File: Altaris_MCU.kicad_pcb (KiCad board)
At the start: 2 copper layers, 101.9 x 50.1 mm, 61 parts, among them J1 Screw_Terminal_01x02, J2 Conn_01x04_Pin, J3 Screw_Terminal_01x02, J4 Screw_Terminal_01x02, J5 Conn_01x04_Pin, J6 Conn_01x04_Pin, J8 Screw_Terminal_01x02, J9 USB_C_Receptacle_USB2.0_16P, SW2 RESET1, SW3 BOOT1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

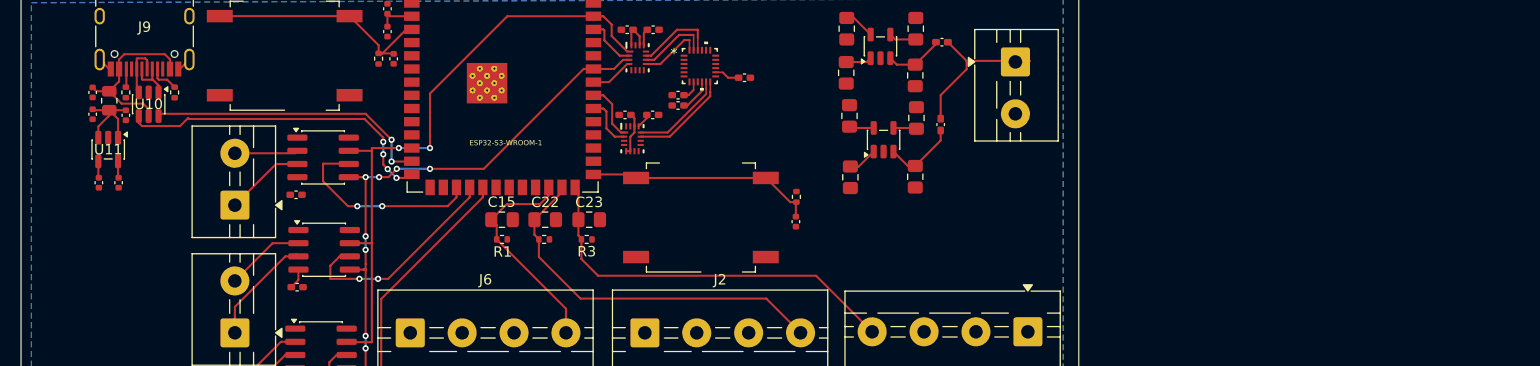
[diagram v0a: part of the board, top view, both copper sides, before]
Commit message: Swapped LDO for Buck and added some test LED's
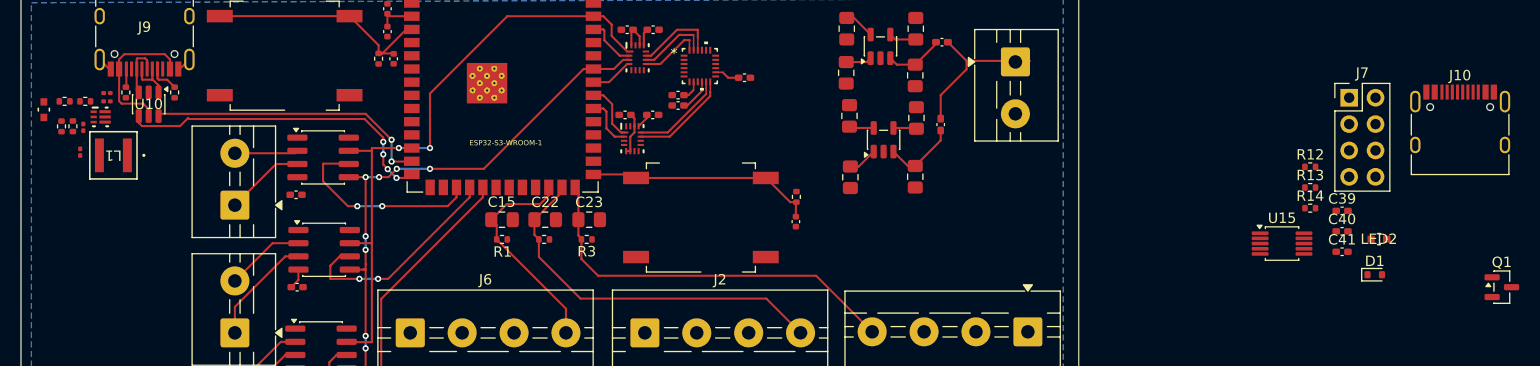
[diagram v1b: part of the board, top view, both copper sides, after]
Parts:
- removed C27, C28, C30: 10u, Capacitor_SMD:C_0402_1005Metric
- removed C29: 100n, Capacitor_SMD:C_0402_1005Metric
- removed FB3: 600/100, Resistor_SMD:R_0805_2012Metric
- removed U11: SPX3819M5-L-3-3, Package_TO_SOT_SMD:SOT-23-5
- added C31: 4.7u, Capacitor_SMD:C_0201_0603Metric, F.Cu at (116.4, 100.1)
- added C32: 30u, Capacitor_SMD:C_0201_0603Metric, F.Cu at (113.8, 105.8)
- added C33: 120p, Capacitor_SMD:C_0201_0603Metric, F.Cu at (114.1, 103.4)
- added C39: 0.1uF, Capacitor_SMD:C_0402_1005Metric_Pad0.74x0.62mm_HandSolder, F.Cu at (235.4, 111.5)
- added C40: 0.1uF, Capacitor_SMD:C_0402_1005Metric_Pad0.74x0.62mm_HandSolder, F.Cu at (235.4, 113.4)
- added C41: 0.1uF, Capacitor_SMD:C_0402_1005Metric_Pad0.74x0.62mm_HandSolder, F.Cu at (235.4, 115.4)
- added D1: 1N4148WT, Diode_SMD:D_SOD-523, F.Cu at (238.5, 117.6)
- added J10: USB_C_Receptacle_USB2.0_16P, Connector_USB:USB_C_Receptacle_HRO_TYPE-C-31-M-12, F.Cu at (246.7, 104.0)
- added J7: Conn_01x08_Socket, Connector_PinHeader_2.54mm:PinHeader_2x04_P2.54mm_Vertical, F.Cu at (236.1, 100.5)
- added L1: 0.47u, MyFootprints:IND_XFL4015_COC, F.Cu at (117.0, 106.1)
- added LED1: LTST-C190KRKT, MyFootprints:LED_LTST-C190_LTO, F.Cu at (110.3, 101.7)
- added LED2: LTST-C190KRKT, MyFootprints:LED_LTST-C190_LTO, F.Cu at (238.9, 114.2)
- added Q1: Q_NMOS, Package_TO_SOT_SMD:SOT-23, F.Cu at (250.8, 118.8)
- added R11: 1k, Resistor_SMD:R_0402_1005Metric, F.Cu at (112.3, 100.9)
- added R12: 1k, Resistor_SMD:R_0402_1005Metric, F.Cu at (232.3, 107.2)
- added R13: 5.1k, Resistor_SMD:R_0402_1005Metric, F.Cu at (232.3, 109.2)
- added R14: 5.1k, Resistor_SMD:R_0402_1005Metric, F.Cu at (232.3, 111.2)
- added R6: 100k, Resistor_SMD:R_0402_1005Metric, F.Cu at (114.3, 100.9)
- added R7: 450k, Resistor_SMD:R_0402_1005Metric, F.Cu at (113.1, 103.3)
- added R8: 100k, Resistor_SMD:R_0402_1005Metric, F.Cu at (112.0, 103.3)
- added U12: TPS62827DMQT, MyFootprints:DMQ0006A, F.Cu at (115.8, 102.4)
- added U15: CH340X, Package_SO:MSOP-10_3x3mm_P0.5mm, F.Cu at (229.6, 114.6)
- C26: value 100n -> 0.1u; footprint Capacitor_SMD:C_0402_1005Metric -> Capacitor_SMD:C_0201_0603Metric
- moved C26 1.63 mm to (116.4, 100.9), turned to 0 degrees
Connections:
- C26 pad 1: +VBUS -> GND
- C26 pad 2: GND -> Net-(U10-VBUS)
- J9 pad A4: +VBUS -> Net-(U10-VBUS)
- J9 pad A9: +VBUS -> Net-(U10-VBUS)
- J9 pad B4: +VBUS -> Net-(U10-VBUS)
- J9 pad B9: +VBUS -> Net-(U10-VBUS)
- U1 pad 23: unconnected-(U1-IO21-Pad23) -> TESTLED
- U1 pad 36: unconnected-(U1-RXD0-Pad36) -> RXD0
- U1 pad 37: unconnected-(U1-TXD0-Pad37) -> TXD0
- U10 pad 5: +VBUS -> Net-(U10-VBUS)
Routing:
- net +VBUS: track 16.6 -> 0.00 mm
- net Net-(U10-VBUS): track 0.00 -> 14.1 mm
- net +VBUSF: track 9.33 -> 0.00 mm
- net Net-(U11-BP): track 1.60 -> 0.00 mm
- net +3.3V_b: track 19.8 -> 18.2 mm

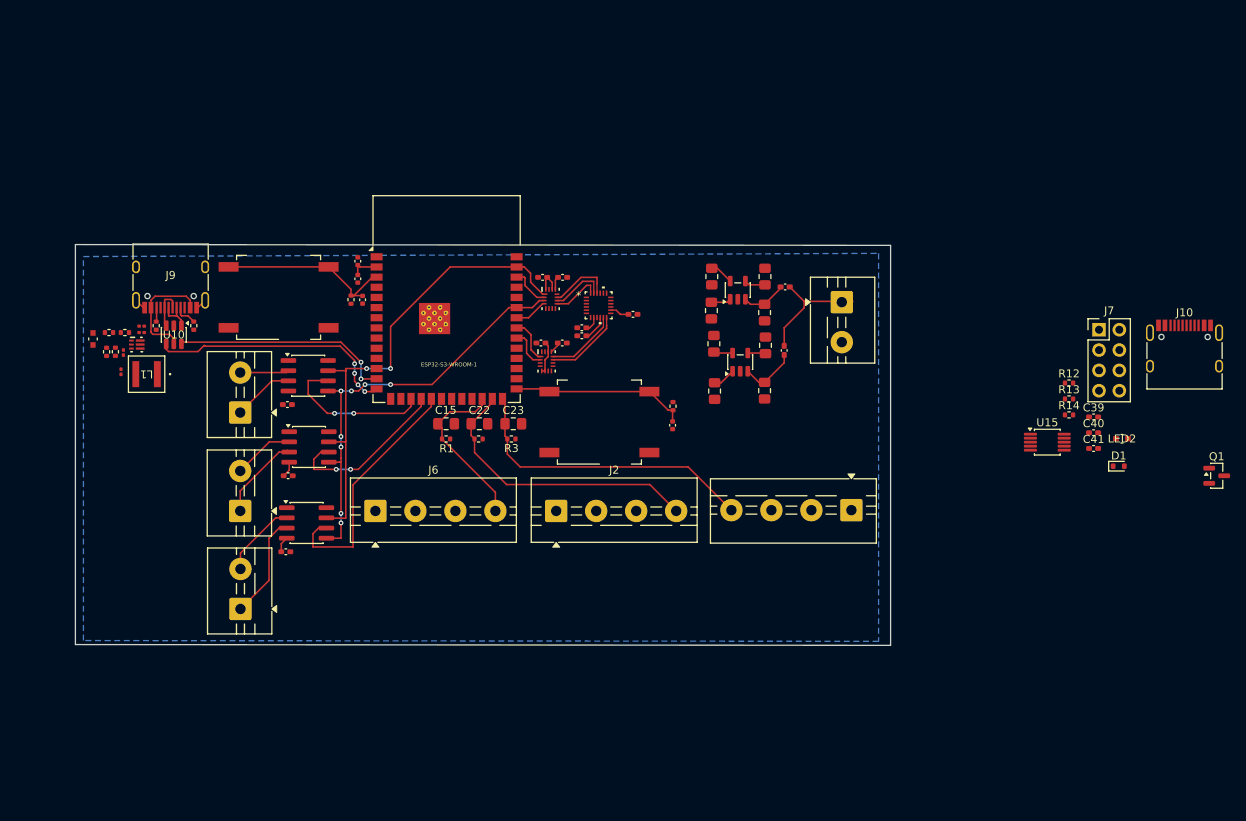
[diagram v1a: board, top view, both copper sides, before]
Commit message: Moved USB-C, Routed Buck converter output to LDO, Removed an LDO on PCB, Added another Thermocouple sensor
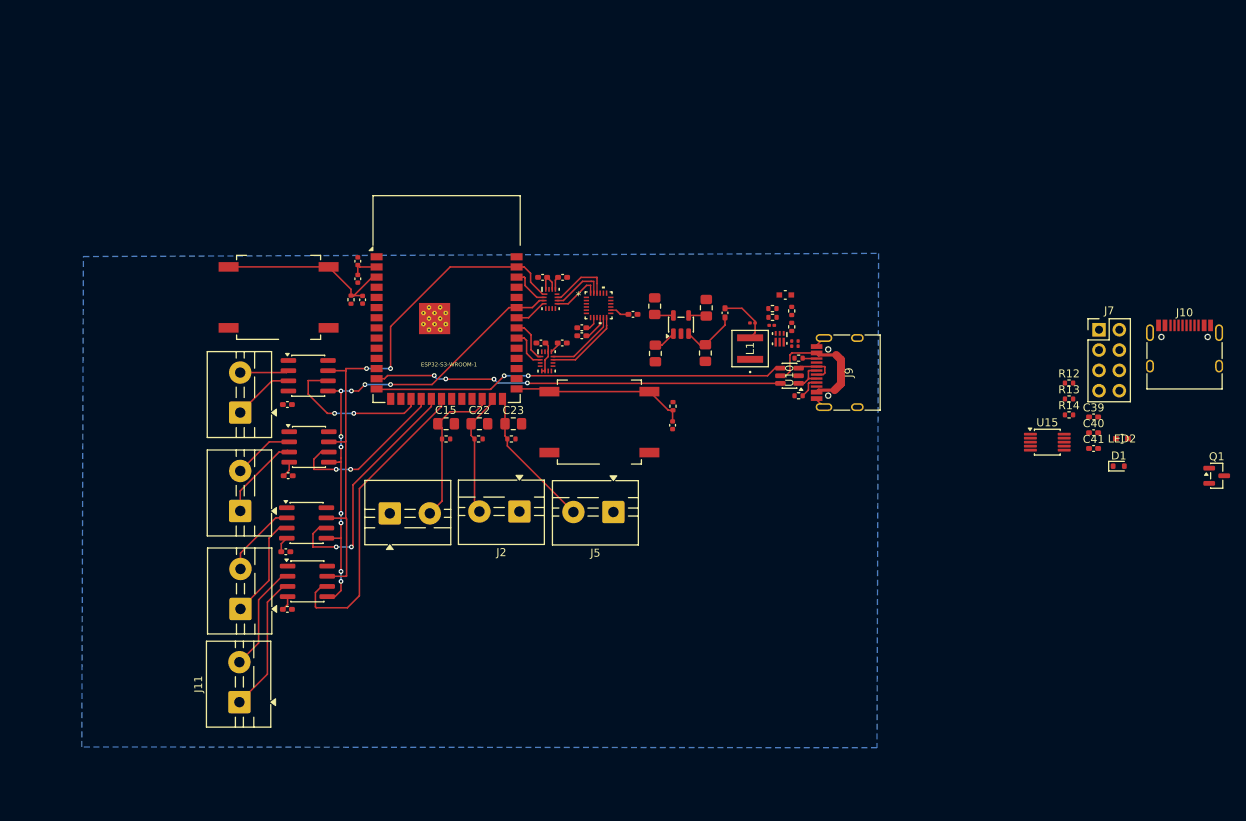
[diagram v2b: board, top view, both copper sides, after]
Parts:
- removed C1: 0.1uF, Capacitor_SMD:C_0805_2012Metric_Pad1.18x1.45mm_HandSolder
- removed C10, C7: 10uF, Capacitor_SMD:C_0805_2012Metric_Pad1.18x1.45mm_HandSolder
- removed C5: 0.01uF, Capacitor_SMD:C_0805_2012Metric_Pad1.18x1.45mm_HandSolder
- removed FB1: 220 @ 100MHz, Inductor_SMD:L_0402_1005Metric_Pad0.77x0.64mm_HandSolder
- removed J8: Screw_Terminal_01x02, TerminalBlock:TerminalBlock_MaiXu_MX126-5.0-02P_1x02_P5.00mm
- removed U3: TPS79333-EP, Package_TO_SOT_SMD:SOT-23-5
- added C27: 0.1uF, Capacitor_SMD:C_0402_1005Metric_Pad0.74x0.62mm_HandSolder, F.Cu at (134.6, 135.5)
- added J11: Screw_Terminal_01x02, TerminalBlock:TerminalBlock_MaiXu_MX126-5.0-02P_1x02_P5.00mm, F.Cu at (128.6, 147.1)
- added U11: MAX31855KASA, Package_SO:SOIC-8_3.9x4.9mm_P1.27mm, F.Cu at (137.1, 132.0)
- J2, J5, J6: footprint TerminalBlock:TerminalBlock_MaiXu_MX126-5.0-04P_1x04_P5.00mm -> TerminalBlock:TerminalBlock_MaiXu_MX126-5.0-02P_1x02_P5.00mm
- moved LED1 86.7 mm to (196.8, 96.2), turned to 0 degrees
- moved J9 85.7 mm to (204.8, 105.9), turned to 90 degrees
- moved R11 85.4 mm to (197.6, 98.2), turned to -90 degrees
- moved R8 83.4 mm to (195.2, 97.9), turned to 0 degrees
- moved R6 83.4 mm to (197.6, 100.2), turned to -90 degrees
- moved R7 82.3 mm to (195.2, 99.0), turned to 180 degrees
- moved C31 82.1 mm to (198.4, 102.3), turned to -90 degrees
- moved C26 81.3 mm to (197.6, 102.3), turned to -90 degrees
- moved C33 81.1 mm to (195.1, 100.0), turned to 0 degrees
- moved R4 80.4 mm to (198.5, 104.1), turned to 180 degrees
- moved U12 80.4 mm to (196.1, 101.7), turned to -90 degrees
- moved C32 79.2 mm to (192.7, 99.7), turned to 180 degrees
- moved U10 77.1 mm to (197.4, 106.3), turned to 180 degrees
- moved R5 76.1 mm to (198.5, 108.8), turned to 180 degrees
- moved L1 75.5 mm to (192.4, 102.9), turned to 90 degrees
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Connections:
- FB2 pad 2: +5V_b -> +3.3V_b
- J2 pad 1: +24V -> Common2
- J2 pad 2: Common2 -> ADC_IN2
- J5 pad 1: +24V -> Common3
- J5 pad 2: Common3 -> ADC_IN3
- J6 pad 1: +24V -> Common1
- J6 pad 2: Common1 -> ADC_IN1
- U1 pad 20: unconnected-(U1-IO12-Pad20) -> MAX_CS4
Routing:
- net MAX_CS4: track 0.00 -> 38.6 mm
- net USB-: track 27.6 -> 51.4 mm, vias 2 -> 4
- net ADC_IN2: track 36.2 -> 15.6 mm
- net ADC_IN3: track 38.1 -> 17.8 mm
- net USB+: track 31.5 -> 51.6 mm, vias 4 -> 2
- net T4+: track 0.00 -> 17.3 mm
- net +5V_b: track 15.2 -> 0.00 mm
- net T4-: track 0.00 -> 13.6 mm
- net MISO: track 60.5 -> 70.2 mm
- net CLK: track 53.5 -> 62.0 mm, vias 8 -> 10
- net Net-(U3-EN): track 8.46 -> 0.00 mm
- net +3.3V_b: track 18.2 -> 23.8 mm
- net Net-(U10-VBUS): track 14.1 -> 16.8 mm
- net Net-(U3-BP): track 2.65 -> 0.00 mm
- net ADC_IN1: track 21.2 -> 19.3 mm
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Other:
- board outline removed

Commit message: Changed to 4 layer board, moved USB-C, rerouted
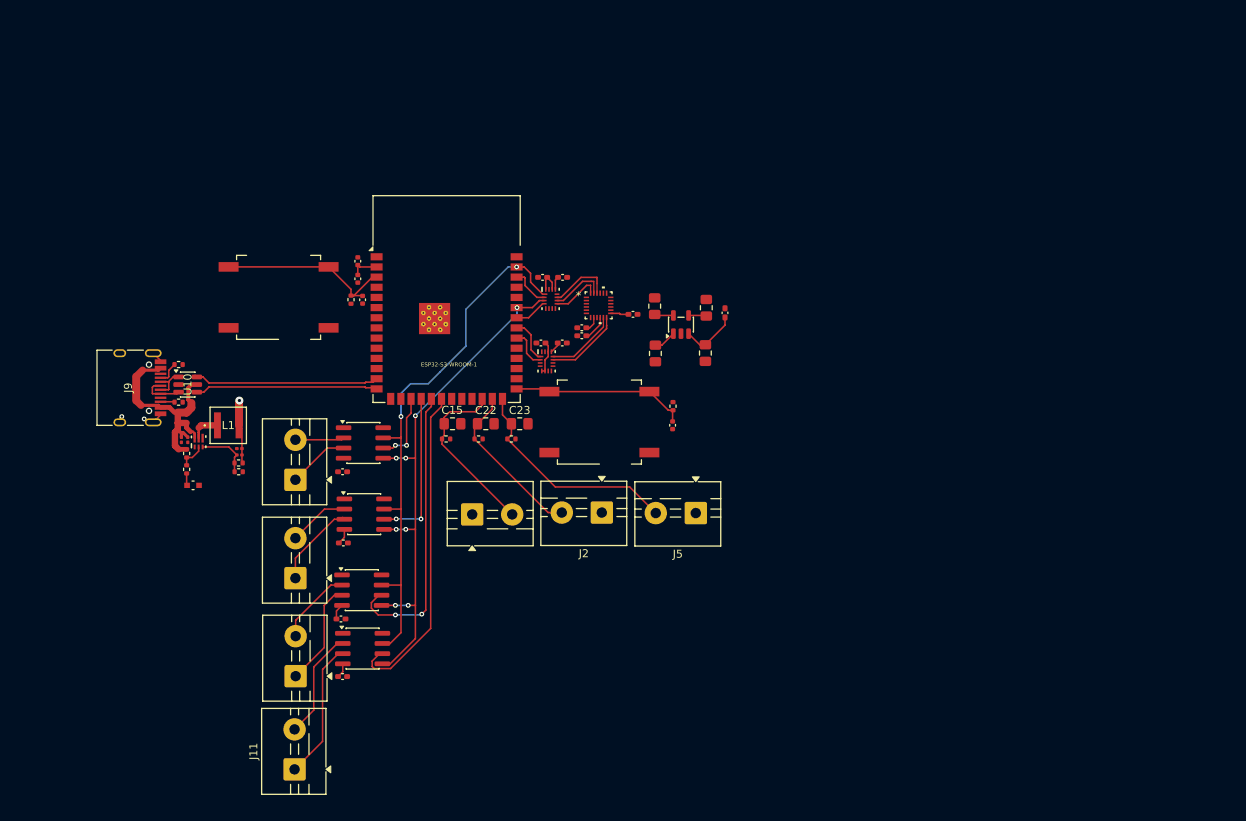
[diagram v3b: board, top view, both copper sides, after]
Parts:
- removed C39, C40, C41: 0.1uF, Capacitor_SMD:C_0402_1005Metric_Pad0.74x0.62mm_HandSolder
- removed D1: 1N4148WT, Diode_SMD:D_SOD-523
- removed J10: USB_C_Receptacle_USB2.0_16P, Connector_USB:USB_C_Receptacle_HRO_TYPE-C-31-M-12
- removed J7: Conn_01x08_Socket, Connector_PinHeader_2.54mm:PinHeader_2x04_P2.54mm_Vertical
- removed LED2: LTST-C190KRKT, MyFootprints:LED_LTST-C190_LTO
- removed Q1: Q_NMOS, Package_TO_SOT_SMD:SOT-23
- removed R12: 1k, Resistor_SMD:R_0402_1005Metric
- removed R13, R14: 5.1k, Resistor_SMD:R_0402_1005Metric
- removed U15: CH340X, Package_SO:MSOP-10_3x3mm_P0.5mm
- moved J9 90.1 mm to (114.7, 107.8), turned to -90 degrees
- moved R11 78.2 mm to (122.0, 118.0), turned to 90 degrees
- moved C31 78.0 mm to (121.3, 114.3), turned to 90 degrees
- moved LED1 77.8 mm to (122.8, 120.0), turned to 180 degrees
- moved R4 77.7 mm to (121.0, 109.6), turned to 0 degrees
- moved R5 77.6 mm to (121.0, 104.9), turned to 0 degrees
- moved R6 77.3 mm to (122.0, 116.0), turned to 90 degrees
- moved C26 76.4 mm to (122.1, 114.3), turned to 90 degrees
- moved U10 75.2 mm to (122.1, 107.4), turned to 0 degrees
- moved U12 73.8 mm to (123.5, 114.5), turned to 90 degrees
- moved R8 69.8 mm to (128.5, 118.3), turned to 180 degrees
- moved R7 69.2 mm to (128.5, 117.2), turned to 0 degrees
- moved C33 68.5 mm to (128.6, 116.2), turned to 180 degrees
- moved C32 66.0 mm to (128.6, 115.4)
- moved L1 65.9 mm to (127.2, 112.5), turned to 0 degrees
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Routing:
- net USB+: track 51.6 -> 22.9 mm, vias 2 -> 0
- net USB-: track 51.4 -> 23.3 mm, vias 4 -> 0
- net Net-(U10-VBUS): track 16.8 -> 29.9 mm
- net ADC_IN3: track 17.8 -> 28.6 mm
- net MAX_CS1: track 19.3 -> 9.16 mm
- net Net-(U12-FB): track 0.00 -> 6.91 mm
- net CLK: track 62.0 -> 68.1 mm, vias 10 -> 8
- net ADC_IN2: track 15.6 -> 21.5 mm
- net MAX_CS3: track 31.1 -> 36.4 mm
- net Net-(U12-SW): track 0.00 -> 3.77 mm
- net Net-(U12-PG): track 0.00 -> 3.33 mm
- net MAX_CS4: track 38.6 -> 41.8 mm
- net ADC_IN1: track 19.3 -> 22.0 mm
- net MISO: track 70.2 -> 68.6 mm
- net Net-(LED1-Pad2): track 0.00 -> 1.51 mm
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- added copper zone on In2.Cu, net +3.3V_b
- added copper zone on In1.Cu, net GND
- removed copper zone on B.Cu, net GND
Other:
- copper layers 2 -> 4

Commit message: added top gnd plane and stitching vias
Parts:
- moved C24 0.68 mm to (166.6, 101.6)
- moved C11 0.62 mm to (177.8, 98.0), turned to 90 degrees
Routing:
- net GND: track 3.72 -> 15.7 mm, vias 2 -> 58
- net +3.3V_b: track 25.0 -> 26.9 mm, vias 1 -> 2
- net +1.8V: track 9.62 -> 10.2 mm
- added copper zone on F.Cu, net GND

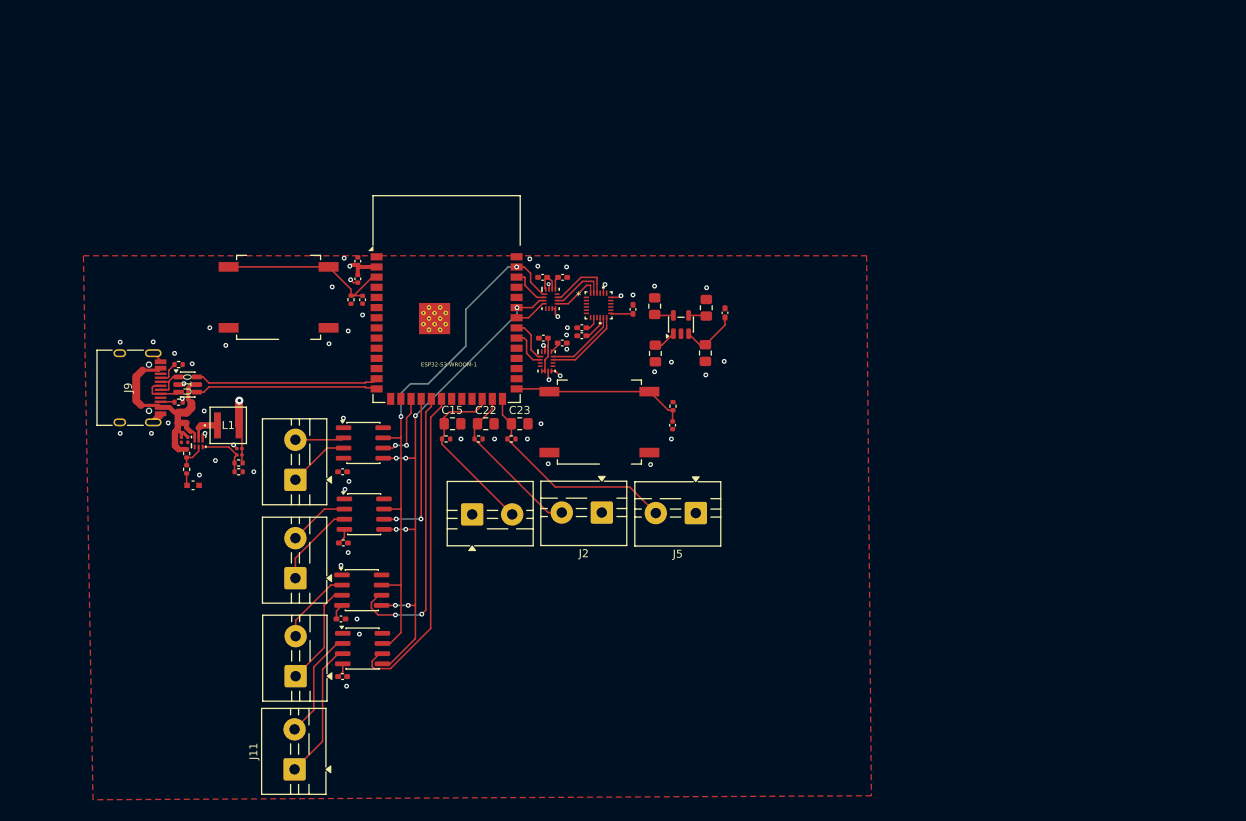
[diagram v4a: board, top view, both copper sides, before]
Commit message: added stitching vias, added power screw terminals
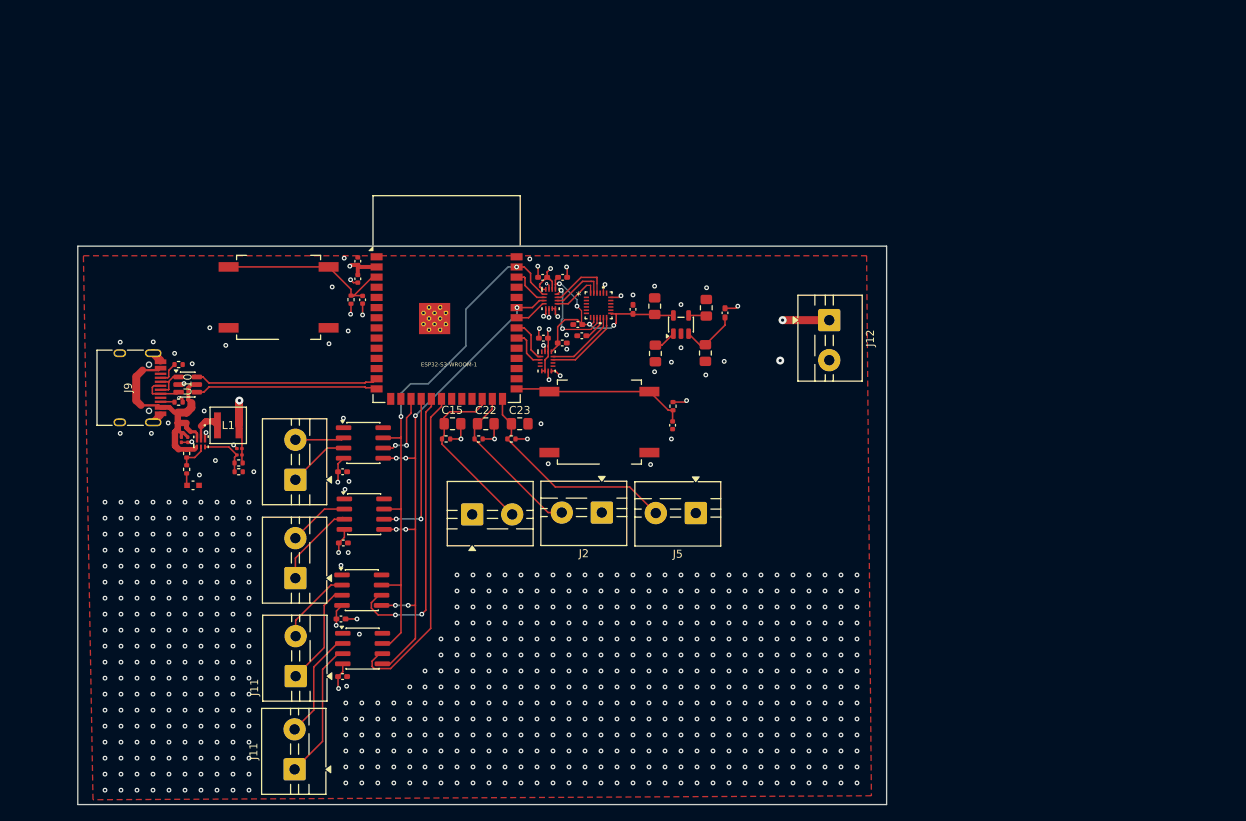
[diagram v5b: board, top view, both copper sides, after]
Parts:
- added J12: Screw_Terminal_01x02, TerminalBlock:TerminalBlock_MaiXu_MX126-5.0-02P_1x02_P5.00mm, F.Cu at (202.3, 99.3)
- moved C12 0.64 mm to (170.9, 99.9)
- moved U12 0.29 mm to (123.8, 114.5)
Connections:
- U12 pad 1: unconnected-(U12-EN-Pad1) -> Net-(U10-VBUS)
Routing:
- net +3.3V_b: track 26.9 -> 50.2 mm, vias 2 -> 14
- net +1.8V: track 10.2 -> 30.8 mm, vias 0 -> 4
- net GND: track 15.7 -> 32.8 mm, vias 58 -> 665
- net ICM_MISO_1.8V: track 0.00 -> 11.1 mm, vias 0 -> 2
- net Net-(U10-VBUS): track 29.9 -> 31.6 mm
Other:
- board outline added: 101.1 x 69.8 mm
- board text added: "J11"
